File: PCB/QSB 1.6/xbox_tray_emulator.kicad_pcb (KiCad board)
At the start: 2 copper layers, 10.2 x 27.7 mm, 6 parts, among them J1 to Xbox, U1 ATtiny13A-S, U2 AP2127N-3.3

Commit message: add net lables, add firmware, update .gitignore
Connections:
- net /Net-(J1-Pad10) renamed /5V
- net /Net-(R1-Pad1) renamed /3V3
- net Net-(C1-Pad2) renamed /GND
- net Net-(J1-Pad4) renamed /NEJECT
- net Net-(J1-Pad5) renamed /TRAY_OUT
- net Net-(J1-Pad6) renamed /CD_RDY
- net Net-(J1-Pad7) renamed /TRAY_IN
- net Net-(J1-Pad8) renamed /SER_DATA
- net Net-(R1-Pad2) renamed /RSET
- J1 pad 1: unconnected-(J1-Pad1) -> /12V
- J1 pad 13: unconnected-(J1-Pad13) -> /NC
- J1 pad 9: unconnected-(J1-Pad9) -> /12V

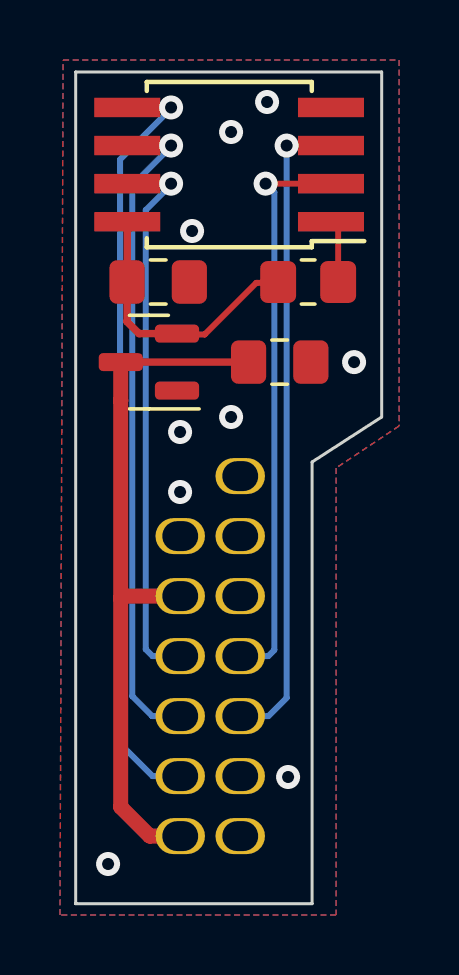
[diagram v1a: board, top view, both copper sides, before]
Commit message: adjust componets locations to make DRC happy, add gerbers.
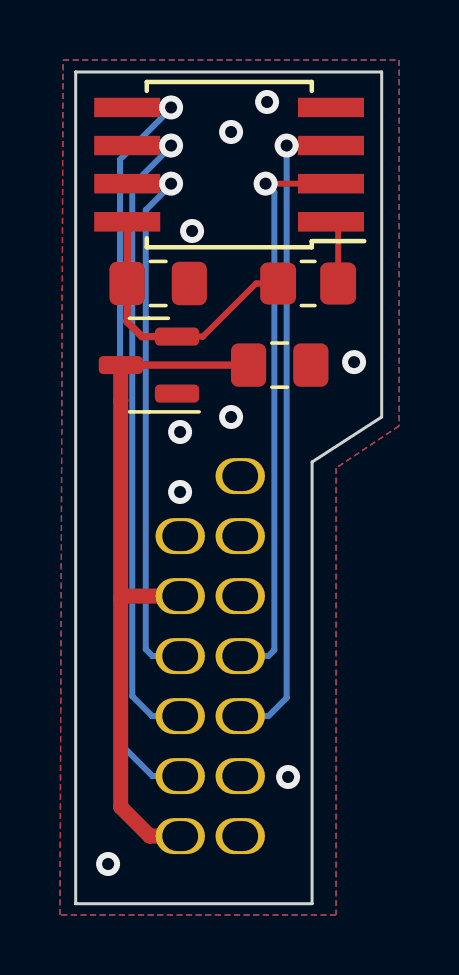
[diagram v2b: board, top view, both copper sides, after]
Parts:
- moved C2 0.10 mm to (143.9, 67.8)
- moved U2 0.10 mm to (139.6, 67.8)
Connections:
- J1 pad 1: /12V -> unconnected-(J1-Pin_1-Pad1)
- J1 pad 9: /12V -> unconnected-(J1-Pin_9-Pad9)
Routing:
- net /3V3: track 9.69 -> 10.3 mm
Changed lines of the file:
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@@
 	(net 5 "/TRAY_IN")
 	(net 6 "/NC")
-	(net 7 "/12V")
+	(net 7 "unconnected-(J1-Pin_9-Pad9)")
 	(net 8 "/NEJECT")
 	(net 9 "/CD_RDY")
 	(net 10 "/TRAY_OUT")
 	(net 11 "/RSET")
+	(net 12 "unconnected-(J1-Pin_1-Pad1)")
 	(footprint "Capacitor_SMD:C_0805_2012Metric_Pad1.18x1.45mm_HandSolder"
 		(layer "F.Cu")
-		(at 139.87 65)
+		(at 139.87 65.05)
 		(descr "Capacitor SMD 0805 (2012 Metric), square (rectangular) end terminal, IPC_7351 nominal with elongated pad for handsoldering. (Body size source: IPC-SM-782 page 76, https://www.pcb-3d.com/wordpress/wp-content/uploads/ipc-sm-782a_amendment_1_and_2.pdf, https://docs.google.com/spreadsheets/d/1BsfQQcO9C6DZCsRaXUlFlo91Tg2WpOkGARC1WS5S8t0/edit?usp=sharing), generated with kicad-footprint-generator")
 		(tags "capacitor handsolder")
@@
 	(footprint "Resistor_SMD:R_0805_2012Metric_Pad1.20x1.40mm_HandSolder"
 		(layer "F.Cu")
-		(at 144.868913 65)
+		(at 144.868913 65.05)
 		(descr "Resistor SMD 0805 (2012 Metric), square (rectangular) end terminal, IPC_7351 nominal with elongated pad for handsoldering. (Body size source: IPC-SM-782 page 72, https://www.pcb-3d.com/wordpress/wp-content/uploads/ipc-sm-782a_amendment_1_and_2.pdf), generated with kicad-footprint-generator")
 		(tags "resistor handsolder")
@@
 	(footprint "Package_TO_SOT_SMD:SOT-23"
 		(layer "F.Cu")
-		(at 139.56 67.67 180)
+		(at 139.56 67.77 180)
 		(descr "SOT, 3 Pin (https://www.jedec.org/system/files/docs/to-236h.pdf variant AB), generated with kicad-footprint-generator ipc_gullwing_generator.py")
 		(tags "SOT TO_SOT_SMD")
@@
 	(footprint "Capacitor_SMD:C_0805_2012Metric_Pad1.18x1.45mm_HandSolder"
 		(layer "F.Cu")
-		(at 143.92 67.67)
+		(at 143.92 67.77)
 		(descr "Capacitor SMD 0805 (2012 Metric), square (rectangular) end terminal, IPC_7351 nominal with elongated pad for handsoldering. (Body size source: IPC-SM-782 page 76, https://www.pcb-3d.com/wordpress/wp-content/uploads/ipc-sm-782a_amendment_1_and_2.pdf, https://docs.google.com/spreadsheets/d/1BsfQQcO9C6DZCsRaXUlFlo91Tg2WpOkGARC1WS5S8t0/edit?usp=sharing), generated with kicad-footprint-generator")
 		(tags "capacitor handsolder")
@@
 			(layers "*.Cu" "*.Mask")
 			(remove_unused_layers no)
-			(net 7 "/12V")
+			(net 12 "unconnected-(J1-Pin_1-Pad1)")
 			(pinfunction "Pin_1")
-			(pintype "passive")
+			(pintype "passive+no_connect")
 		)
 		(pad "2" thru_hole oval
@@
 			(layers "*.Cu" "*.Mask")
 			(remove_unused_layers no)
-			(net 7 "/12V")
+			(net 7 "unconnected-(J1-Pin_9-Pad9)")
 			(pinfunction "Pin_9")
-			(pintype "passive")
+			(pintype "passive+no_connect")
 		)
 		(pad "10" thru_hole oval
@@
 	)
 	(segment
-		(start 139.23 66.72)
+		(start 143.13 65.05)
+		(end 143.868913 65.05)
+		(width 0.2)
+		(layer "F.Cu")
+		(net 2)
+	)
+	(segment
+		(start 140.4975 66.82)
+		(end 141.36 66.82)
+		(width 0.2)
+		(layer "F.Cu")
+		(net 2)
+	)
+	(segment
+		(start 141.36 66.82)
+		(end 143.13 65.05)
+		(width 0.2)
+		(layer "F.Cu")
+		(net 2)
+	)
+	(segment
+		(start 138.84 64.9925)
+		(end 138.8325 65)
+		(width 0.25)
+		(layer "F.Cu")
+		(net 2)
+	)
+	(segment
+		(start 139.33 66.82)
+		(end 140.3975 66.82)
+		(width 0.25)
+		(layer "F.Cu")
+		(net 2)
+	)
+	(segment
+		(start 140.3975 66.82)
 		(end 140.4975 66.72)
+		(width 0.25)
+		(layer "F.Cu")
+		(net 2)
+	)
+	(segment
+		(start 138.84 62.992)
+		(end 138.84 64.9925)
 		(width 0.25)
 		(layer "F.Cu")
@@
 	)
 	(segment
-		(start 143.868913 65.028433)
-		(end 143.141567 65.028433)
-		(width 0.2)
-		(layer "F.Cu")
-		(net 2)
-	)
-	(segment
-		(start 138.8325 66.3225)
-		(end 139.23 66.72)
-		(width 0.25)
-		(layer "F.Cu")
-		(net 2)
-	)
-	(segment
-		(start 143.141567 65.028433)
-		(end 141.42 66.75)
-		(width 0.2)
-		(layer "F.Cu")
-		(net 2)
-	)
-	(segment
-		(start 138.84 64.9925)
-		(end 138.8325 65)
-		(width 0.25)
-		(layer "F.Cu")
-		(net 2)
-	)
-	(segment
-		(start 138.84 62.992)
-		(end 138.84 64.9925)
-		(width 0.25)
-		(layer "F.Cu")
-		(net 2)
-	)
-	(segment
-		(start 141.42 66.75)
-		(end 141.0375 66.75)
-		(width 0.2)
-		(layer "F.Cu")
-		(net 2)
-	)
-	(segment
 		(start 141.0375 66.75)
 		(end 140.06 66.75)
@@
 	)
 	(segment
+		(start 138.8325 66.3225)
+		(end 139.33 66.82)
+		(width 0.25)
+		(layer "F.Cu")
+		(net 2)
+	)
+	(segment
 		(start 138.62 75.54)
 		(end 138.69 75.47)
@@
 	)
 	(segment
+		(start 138.62 75.54)
+		(end 138.62 68.95)
+		(width 0.5)
+		(layer "F.Cu")
+		(net 3)
+	)
+	(segment
+		(start 138.6225 68.9475)
+		(end 138.6225 67.77)
+		(width 0.5)
+		(layer "F.Cu")
+		(net 3)
+	)
+	(segment
+		(start 138.69 75.47)
+		(end 140.605 75.47)
+		(width 0.5)
+		(layer "F.Cu")
+		(net 3)
+	)
+	(segment
+		(start 138.62 82.5)
+		(end 138.62 75.54)
+		(width 0.5)
+		(layer "F.Cu")
+		(net 3)
+	)
+	(segment
+		(start 139.59 83.47)
+		(end 138.62 82.5)
+		(width 0.5)
+		(layer "F.Cu")
+		(net 3)
+	)
+	(segment
+		(start 140.605 83.47)
+		(end 139.59 83.47)
+		(width 0.5)
+		(layer "F.Cu")
+		(net 3)
+	)
+	(segment
 		(start 138.62 68.95)
 		(end 138.6225 68.9475)
@@
 	)
 	(segment
-		(start 138.6225 68.9475)
-		(end 138.6225 67.67)
-		(width 0.5)
-		(layer "F.Cu")
-		(net 3)
-	)
-	(segment
-		(start 138.69 75.47)
-		(end 140.605 75.47)
-		(width 0.5)
-		(layer "F.Cu")
-		(net 3)
-	)
-	(segment
-		(start 138.62 82.5)
-		(end 138.62 75.54)
-		(width 0.5)
-		(layer "F.Cu")
-		(net 3)
-	)
-	(segment
-		(start 139.59 83.47)
-		(end 138.62 82.5)
-		(width 0.5)
-		(layer "F.Cu")
-		(net 3)
-	)
-	(segment
-		(start 140.605 83.47)
-		(end 139.59 83.47)
-		(width 0.5)
-		(layer "F.Cu")
-		(net 3)
-	)
-	(segment
-		(start 138.62 75.54)
-		(end 138.62 68.95)
-		(width 0.5)
-		(layer "F.Cu")
-		(net 3)
-	)
-	(segment
-		(start 142.7425 67.67)
-		(end 138.6225 67.67)
+		(start 142.7425 67.77)
+		(end 138.6225 67.77)
 		(width 0.25)
 		(layer "F.Cu")
